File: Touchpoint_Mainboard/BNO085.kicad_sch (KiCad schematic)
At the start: 16 parts, among them U8 BNO055, Y2 Crystal

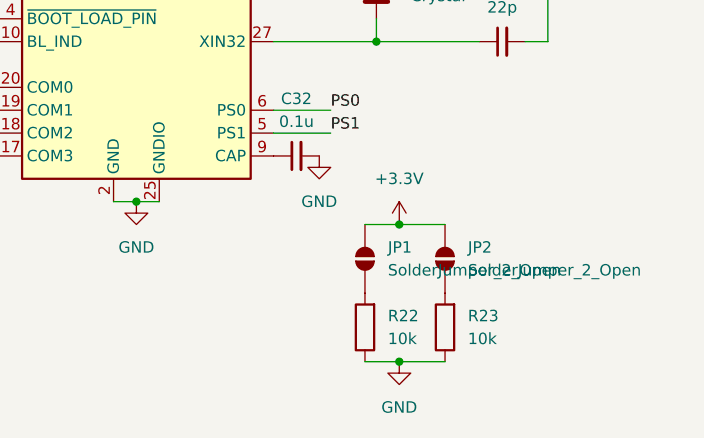
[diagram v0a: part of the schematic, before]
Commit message: FInished populating mainboard schematic
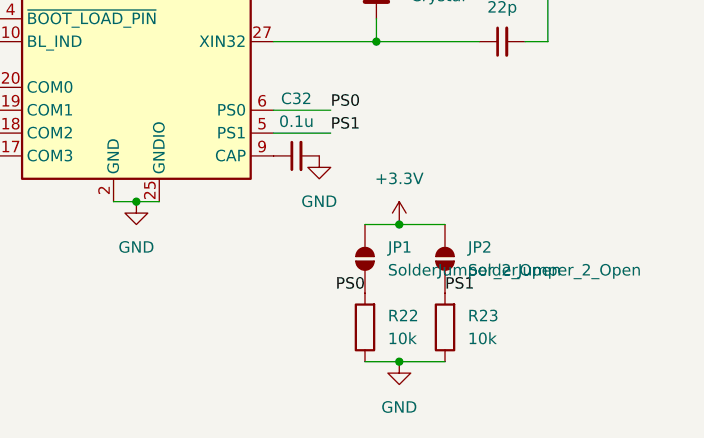
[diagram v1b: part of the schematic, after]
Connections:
- net PS0: now also JP1.1 (A), R22.2
- net PS1: now also JP2.1 (A), R23.2
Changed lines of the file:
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@@
+		)
+	)
+	(label "PS0"
+		(at 102.87 92.71 180)
+		(effects
+			(font
+				(size 1.27 1.27)
+			)
+			(justify right bottom)
+		)
+	)
+	(label "PS1"
+		(at 111.76 92.71 0)
+		(effects
+			(font
+				(size 1.27 1.27)
+			)
+			(justify left bottom)
 		)
 	)

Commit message: Finished assigning most footprints
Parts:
- C31, C32, C33, C34: footprint (none) -> Capacitor_SMD:C_0402_1005Metric
- JP1, JP2: footprint (none) -> Jumper:SolderJumper-2_P1.3mm_Open_RoundedPad1.0x1.5mm
- R16, R17, R18, R19, R20, R21, R22, R23: footprint (none) -> Resistor_SMD:R_0402_1005Metric
- Y2: footprint (none) -> Touchpoint:XTAL_MU00525_NDK
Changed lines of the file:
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@@
 			)
 		)
-		(property "Footprint" ""
+		(property "Footprint" "Touchpoint:XTAL_MU00525_NDK"
 			(at 104.14 58.42 0)
 			(effects
@@
 			)
 		)
-		(property "Footprint" ""
+		(property "Footprint" "Capacitor_SMD:C_0402_1005Metric"
 			(at 118.11 64.77 0)
 			(effects
@@
 			)
 		)
-		(property "Footprint" ""
+		(property "Footprint" "Resistor_SMD:R_0402_1005Metric"
 			(at 41.91 94.488 90)
 			(effects
@@
 			)
 		)
-		(property "Footprint" ""
+		(property "Footprint" "Jumper:SolderJumper-2_P1.3mm_Open_RoundedPad1.0x1.5mm"
 			(at 111.76 88.9 0)
 			(effects
@@
 			)
 		)
-		(property "Footprint" ""
+		(property "Footprint" "Jumper:SolderJumper-2_P1.3mm_Open_RoundedPad1.0x1.5mm"
 			(at 102.87 88.9 0)
 			(effects
@@
 			)
 		)
-		(property "Footprint" ""
+		(property "Footprint" "Resistor_SMD:R_0402_1005Metric"
 			(at 41.91 88.138 90)
 			(effects
@@
 			)
 		)
-		(property "Footprint" ""
+		(property "Footprint" "Capacitor_SMD:C_0402_1005Metric"
 			(at 118.11 52.07 0)
 			(effects
@@
 			)
 		)
-		(property "Footprint" ""
+		(property "Footprint" "Resistor_SMD:R_0402_1005Metric"
 			(at 41.91 102.108 90)
 			(effects
@@
 			)
 		)
-		(property "Footprint" ""
+		(property "Footprint" "Resistor_SMD:R_0402_1005Metric"
 			(at 41.91 76.708 90)
 			(effects
@@
 			)
 		)
-		(property "Footprint" ""
+		(property "Footprint" "Capacitor_SMD:C_0402_1005Metric"
 			(at 95.25 77.47 0)
 			(effects
@@
 			)
 		)
-		(property "Footprint" ""
+		(property "Footprint" "Resistor_SMD:R_0402_1005Metric"
 			(at 104.648 96.52 90)
 			(effects
@@
 			)
 		)
-		(property "Footprint" ""
+		(property "Footprint" "Resistor_SMD:R_0402_1005Metric"
 			(at 41.91 53.848 90)
 			(effects
@@
 			)
 		)
-		(property "Footprint" ""
+		(property "Footprint" "Resistor_SMD:R_0402_1005Metric"
 			(at 113.538 96.52 90)
 			(effects
@@
 			)
 		)
-		(property "Footprint" ""
+		(property "Footprint" "Resistor_SMD:R_0402_1005Metric"
 			(at 41.91 64.008 90)
 			(effects
@@
 			)
 		)
-		(property "Footprint" ""
+		(property "Footprint" "Capacitor_SMD:C_0402_1005Metric"
 			(at 72.39 43.18 0)
 			(effects

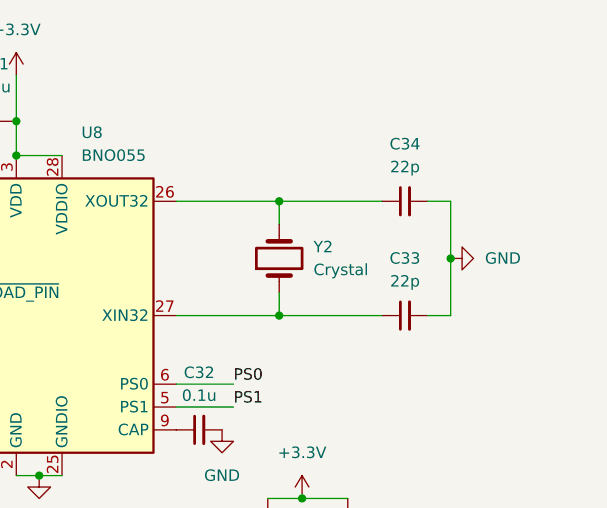
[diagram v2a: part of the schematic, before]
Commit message: Changed some component values based on availability
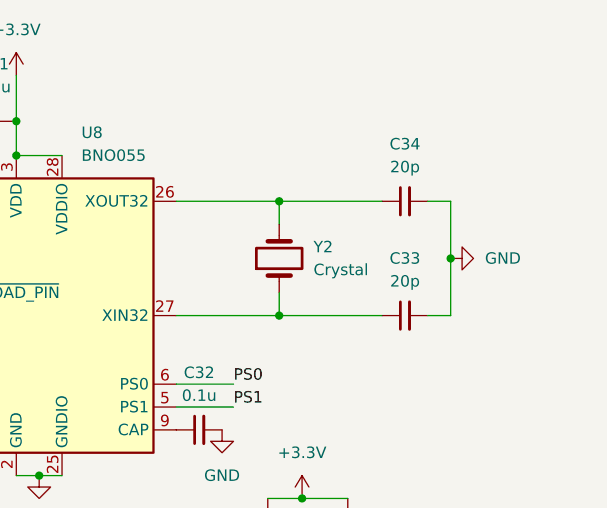
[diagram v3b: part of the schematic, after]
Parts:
- C33, C34: value 22p -> 20p
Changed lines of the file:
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@@
 			)
 		)
-		(property "Value" "22p"
+		(property "Value" "20p"
 			(at 118.1163 60.96 90)
 			(effects
@@
 			)
 		)
-		(property "Value" "22p"
+		(property "Value" "20p"
 			(at 118.1163 48.26 90)
 			(effects

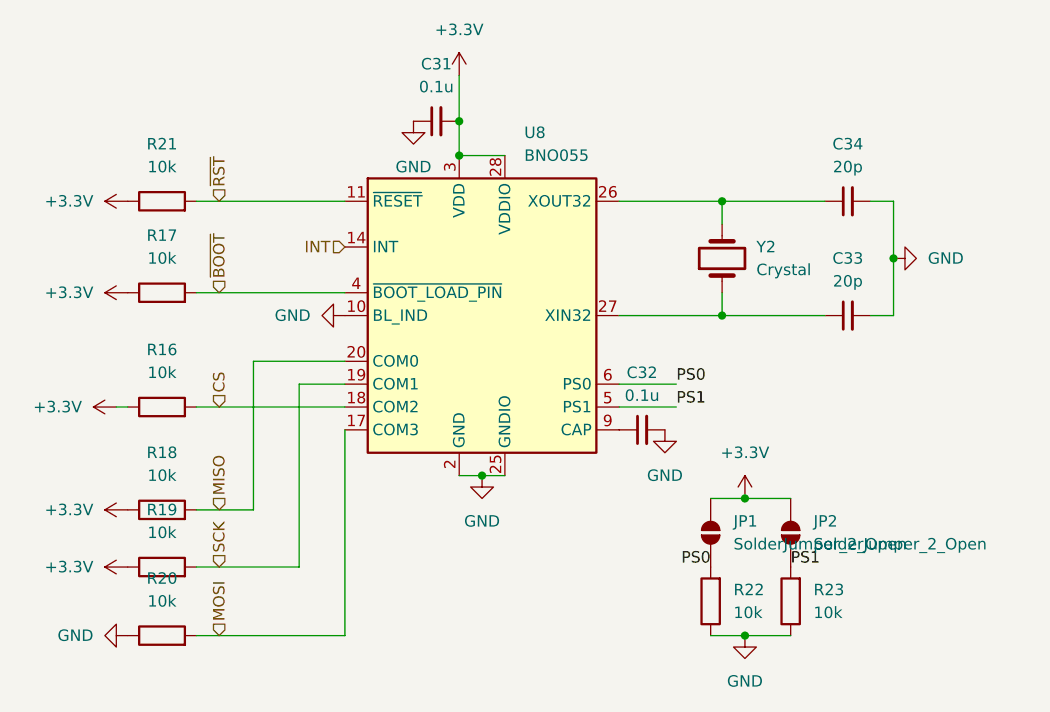
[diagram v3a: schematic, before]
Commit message: Added 3.3V to interface
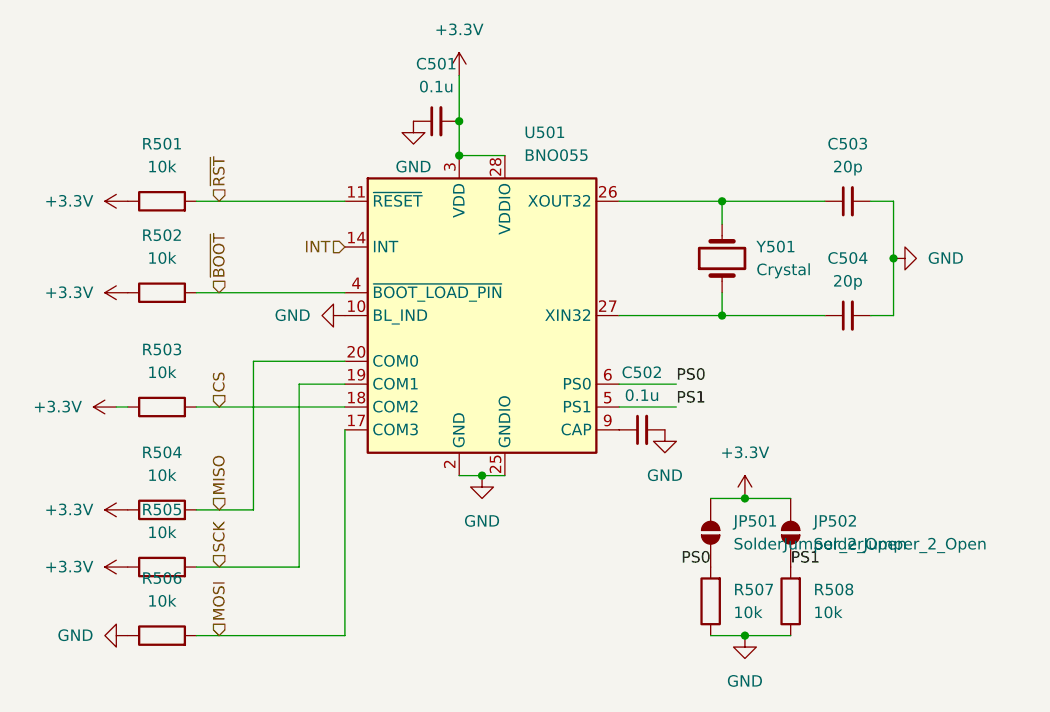
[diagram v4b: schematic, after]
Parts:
- renumbered C31 to C501, C32 to C502, C34 to C503, C33 to C504, JP1 to JP501, JP2 to JP502, R21 to R501, R17 to R502, R16 to R503, R18 to R504, R19 to R505, R20 to R506, R22 to R507, R23 to R508, U8 to U501, Y2 to Y501
